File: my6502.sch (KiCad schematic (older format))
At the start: 4 parts

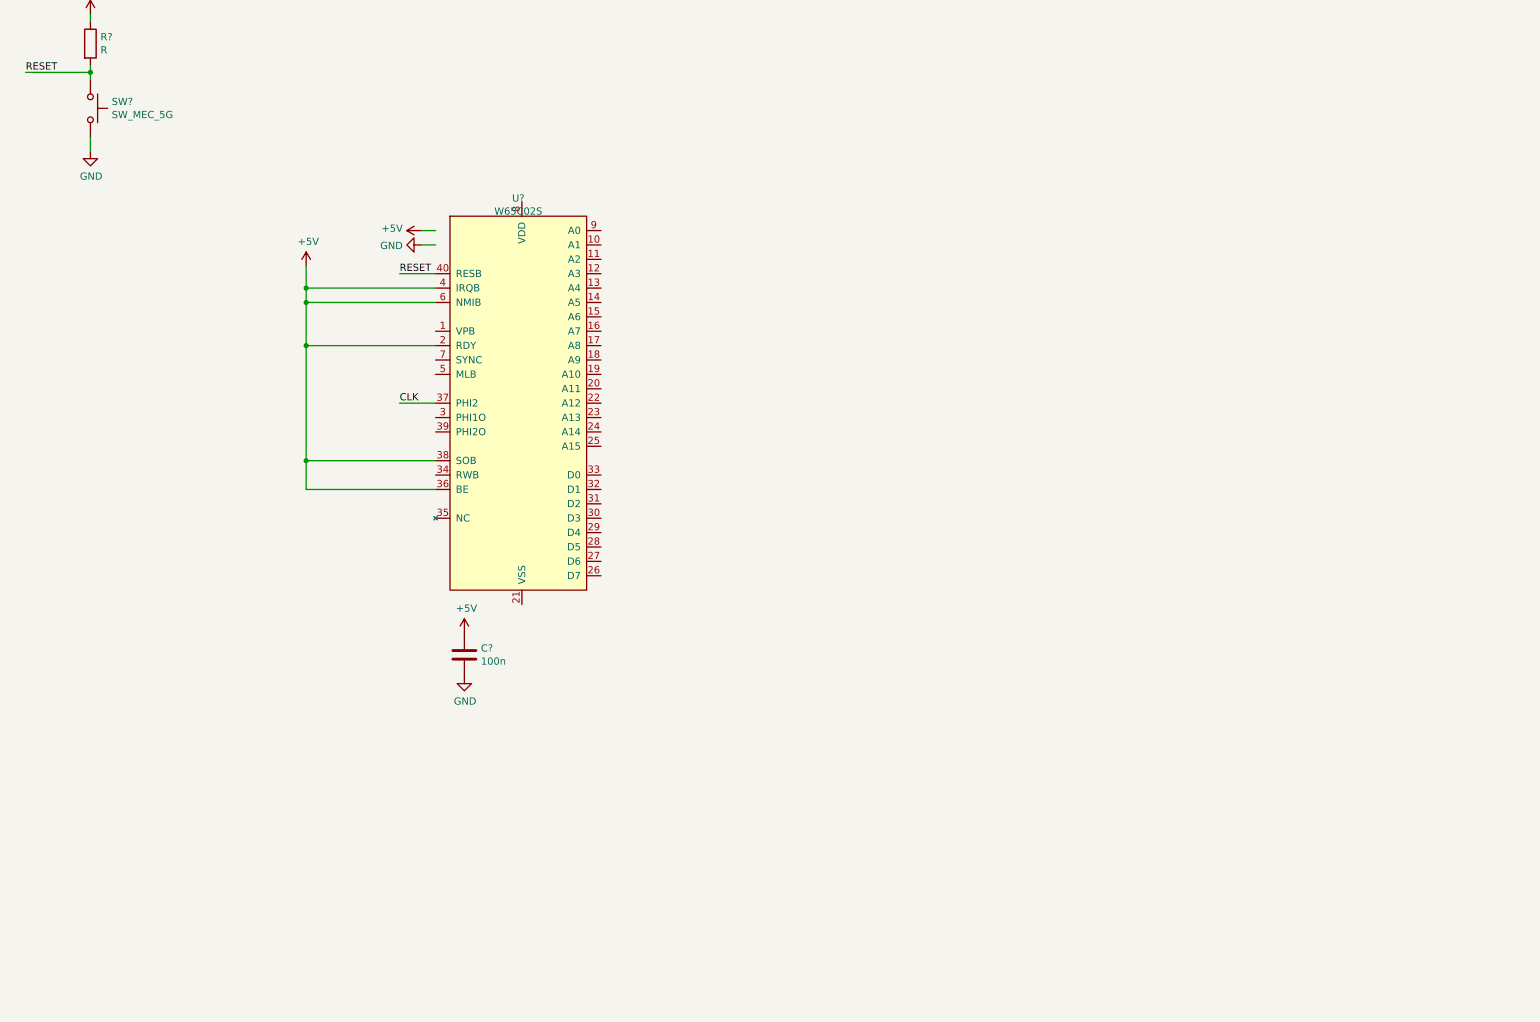
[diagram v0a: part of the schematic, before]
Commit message: Added VIA 65C22
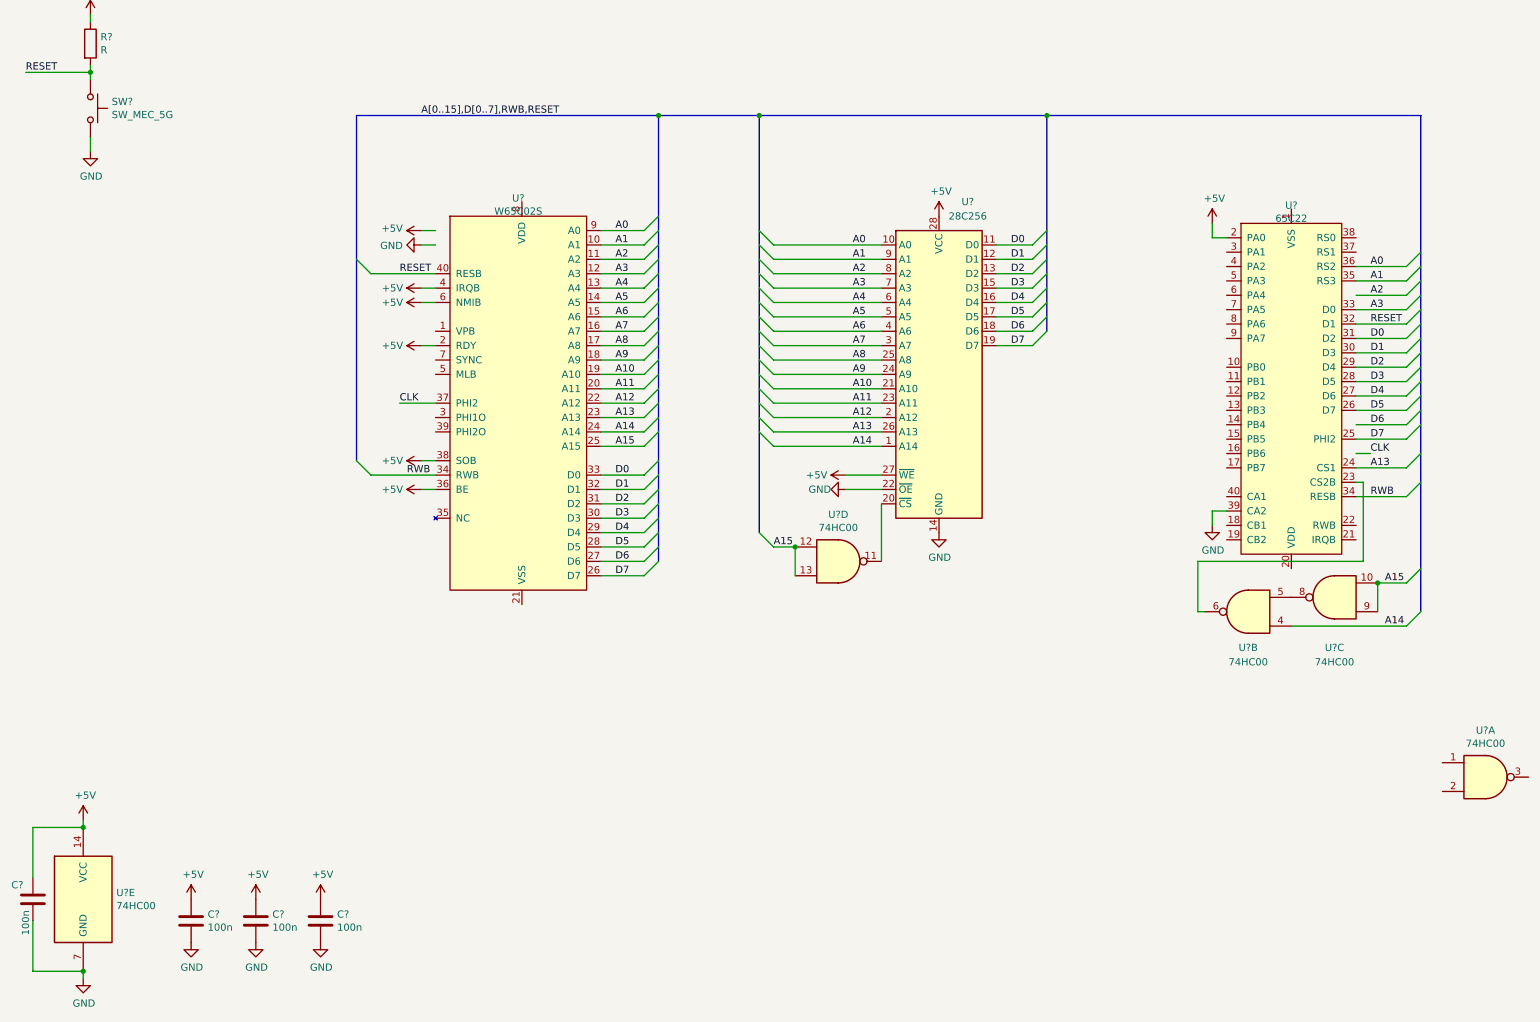
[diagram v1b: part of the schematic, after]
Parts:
- added C? (x3): 100n, symbol Device:C
- added U?: 28C256, symbol Memory_EEPROM:28C256
- added U? (x5): 74HC00, symbol 74xx:74HC00
- added U?: 65C22, symbol 6502:65C22
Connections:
- net labels added: A0, A1, A10, A11, A12, A13, A14, A15, A2, A3, A4, A5, A6, A7, A8, A9, A[0..15],D[0..7],RWB,RESET, D0, D1, D2, D3, D4, D5, D6, D7, RWB
- wire segments 19 -> 101
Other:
- moved on the sheet: C?

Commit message: Add RAM
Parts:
- removed U?: 74HC00, symbol 74xx:74HC00
- added C?: 100n, symbol Device:C
- added U?: CY62256-70PC, Package_DIP:DIP-28_W15.24mm, symbol Memory_RAM:CY62256-70PC
- added U?: 74HC00, symbol 74xx:74HC00
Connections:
- net labels added: ~A15
- wire segments 101 -> 141
- no-connect marks 0 -> 1
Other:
- moved on the sheet: R?, SW?, U?, U?A, U?B, U?D

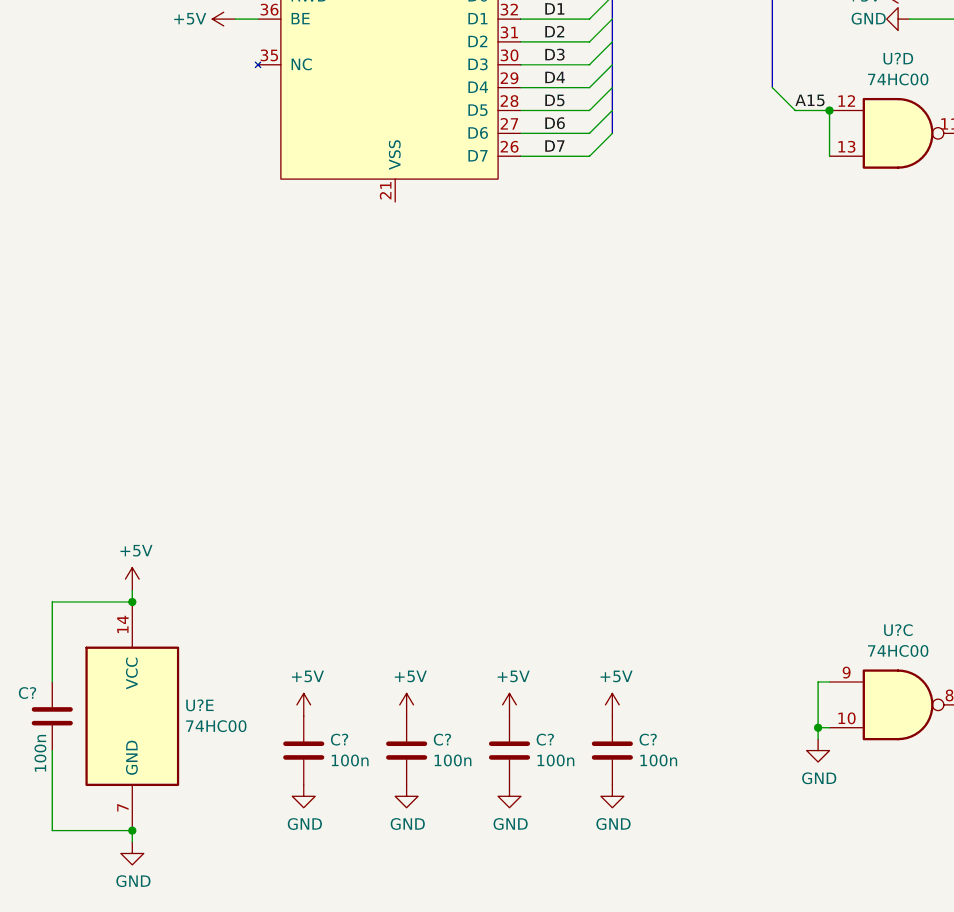
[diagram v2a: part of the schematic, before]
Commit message: Add minimal 555-based clock module
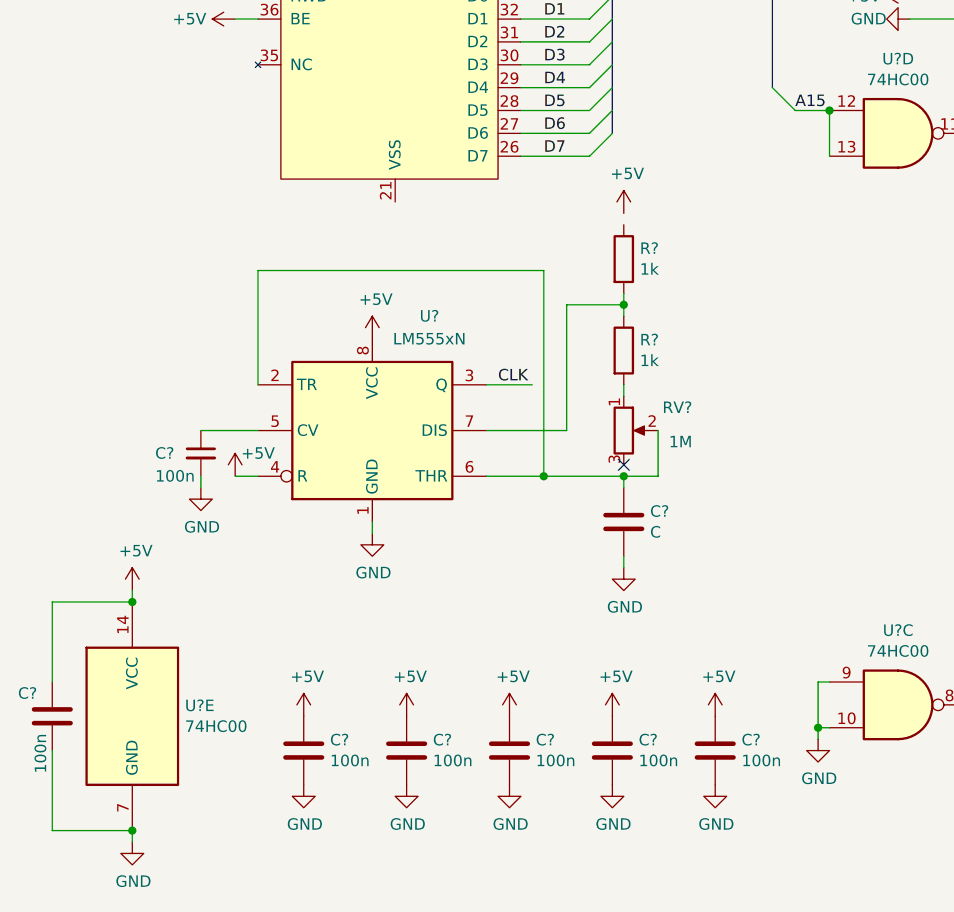
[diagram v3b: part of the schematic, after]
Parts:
- added C?: 100n, symbol Device:C
- added C?: 100n, symbol Device:C_Small
- added C?: C, symbol Device:C
- added R? (x2): 1k, symbol Device:R
- added RV?: 1M, symbol Device:R_POT
- added U?: LM555xN, Package_DIP:DIP-8_W7.62mm, symbol Timer:LM555xN
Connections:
- wire segments 141 -> 161
- no-connect marks 1 -> 2
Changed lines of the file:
@@
 Connection ~ 4050 7000
 NoConn ~ 4700 6900
+$Comp
+L Timer:LM555xN U?
+U 1 1 600B01EE
+P 2100 5700
+F 0 "U?" H 2350 6200 50  0000 C CNN
+F 1 "LM555xN" H 2350 6100 50  0000 C CNN
+F 2 "Package_DIP:DIP-8_W7.62mm" H 2750 5300 50  0001 C CNN
+F 3 "http://www.ti.com/lit/ds/symlink/lm555.pdf" H 2950 5300 50  0001 C CNN
+	1    2100 5700
+	1    0    0    -1
+$EndComp
+$Comp
+L power:+5V #PWR?
+U 1 1 600BEA22
+P 3200 4750
+F 0 "#PWR?" H 3200 4600 50  0001 C CNN
+F 1 "+5V" H 3215 4923 50  0000 C CNN
+F 2 "" H 3200 4750 50  0001 C CNN
+F 3 "" H 3200 4750 50  0001 C CNN
+	1    3200 4750
+	1    0    0    -1
+$EndComp
+Wire Wire Line
+	1600 5500 1600 5000
+Wire Wire Line
+	1600 5000 2850 5000
+Wire Wire Line
+	2850 5000 2850 5900
+$Comp
+L power:GND #PWR?
+U 1 1 601152B0
+P 3200 6300
+F 0 "#PWR?" H 3200 6050 50  0001 C CNN
+F 1 "GND" H 3205 6127 50  0000 C CNN
+F 2 "" H 3200 6300 50  0001 C CNN
+F 3 "" H 3200 6300 50  0001 C CNN
+	1    3200 6300
+	1    0    0    -1
+$EndComp
+$Comp
+L power:+5V #PWR?
+U 1 1 601169B4
+P 2100 5300
+F 0 "#PWR?" H 2100 5150 50  0001 C CNN
+F 1 "+5V" H 2115 5473 50  0000 C CNN
+F 2 "" H 2100 5300 50  0001 C CNN
+F 3 "" H 2100 5300 50  0001 C CNN
+	1    2100 5300
+	1    0    0    -1
+$EndComp
+$Comp
+L power:GND #PWR?
+U 1 1 6011DD9C
+P 2100 6150
+F 0 "#PWR?" H 2100 5900 50  0001 C CNN
+F 1 "GND" H 2105 5977 50  0000 C CNN
+F 2 "" H 2100 6150 50  0001 C CNN
+F 3 "" H 2100 6150 50  0001 C CNN
+	1    2100 6150
+	1    0    0    -1
+$EndComp
+$Comp
+L power:+5V #PWR?
+U 1 1 6012E6E9
+P 3600 6950
+F 0 "#PWR?" H 3600 6800 50  0001 C CNN
+F 1 "+5V" H 3615 7123 50  0000 C CNN
+F 2 "" H 3600 6950 50  0001 C CNN
+F 3 "" H 3600 6950 50  0001 C CNN
+	1    3600 6950
+	1    0    0    -1
+$EndComp
+$Comp
+L power:GND #PWR?
+U 1 1 6012EA99
+P 3600 7250
+F 0 "#PWR?" H 3600 7000 50  0001 C CNN
+F 1 "GND" H 3605 7077 50  0000 C CNN
+F 2 "" H 3600 7250 50  0001 C CNN
+F 3 "" H 3600 7250 50  0001 C CNN
+	1    3600 7250
+	1    0    0    -1
+$EndComp
+$Comp
+L Device:C C?
+U 1 1 6012EAA3
+P 3600 7100
+F 0 "C?" H 3715 7146 50  0000 L CNN
+F 1 "100n" H 3715 7055 50  0000 L CNN
+F 2 "" H 3638 6950 50  0001 C CNN
+F 3 "~" H 3600 7100 50  0001 C CNN
+	1    3600 7100
+	1    0    0    -1
+$EndComp
+$Comp
+L Device:C_Small C?
+U 1 1 6018E46C
+P 1350 5800
+F 0 "C?" H 1150 5800 50  0000 L CNN
+F 1 "100n" H 1150 5700 50  0000 L CNN
+F 2 "" H 1350 5800 50  0001 C CNN
+F 3 "~" H 1350 5800 50  0001 C CNN
+	1    1350 5800
+	1    0    0    -1
+$EndComp
+$Comp
+L power:GND #PWR?
+U 1 1 6018F461
+P 1350 5950
+F 0 "#PWR?" H 1350 5700 50  0001 C CNN
+F 1 "GND" H 1355 5777 50  0000 C CNN
+F 2 "" H 1350 5950 50  0001 C CNN
+F 3 "" H 1350 5950 50  0001 C CNN
+	1    1350 5950
+	1    0    0    -1
+$EndComp
+Wire Wire Line
+	1350 5700 1600 5700
+Wire Wire Line
+	1350 5900 1350 5950
+$Comp
+L power:+5V #PWR?
+U 1 1 601B5080
+P 1500 5900
+F 0 "#PWR?" H 1500 5750 50  0001 C CNN
+F 1 "+5V" H 1600 6000 50  0000 C CNN
+F 2 "" H 1500 5900 50  0001 C CNN
+F 3 "" H 1500 5900 50  0001 C CNN
+	1    1500 5900
+	1    0    0    -1
+$EndComp
+Wire Wire Line
+	1500 5900 1600 5900
+Wire Wire Line
+	2100 6100 2100 6150
+$Comp
+L Device:R_POT RV?
+U 1 1 601E869A
+P 3200 5700
+F 0 "RV?" H 3500 5800 50  0000 R CNN
+F 1 "1M" H 3500 5650 50  0000 R CNN
+F 2 "" H 3200 5700 50  0001 C CNN
+F 3 "~" H 3200 5700 50  0001 C CNN
+	1    3200 5700
+	1    0    0    -1
+$EndComp
+$Comp
+L Device:R R?
+U 1 1 601F2A63
+P 3200 5350
+F 0 "R?" H 3270 5396 50  0000 L CNN
+F 1 "1k" H 3270 5305 50  0000 L CNN
+F 2 "" V 3130 5350 50  0001 C CNN
+F 3 "~" H 3200 5350 50  0001 C CNN
+	1    3200 5350
+	1    0    0    -1
+$EndComp
+$Comp
+L Device:R R?
+U 1 1 601F2D27
+P 3200 4950
+F 0 "R?" H 3270 4996 50  0000 L CNN
+F 1 "1k" H 3270 4905 50  0000 L CNN
+F 2 "" V 3130 4950 50  0001 C CNN
+F 3 "~" H 3200 4950 50  0001 C CNN
+	1    3200 4950
+	1    0    0    -1
+$EndComp
+Wire Wire Line
+	2600 5900 2850 5900
+$Comp
+L Device:C C?
+U 1 1 601F897F
+P 3200 6100
+F 0 "C?" H 3315 6146 50  0000 L CNN
+F 1 "C" H 3315 6055 50  0000 L CNN
+F 2 "" H 3238 5950 50  0001 C CNN
+F 3 "~" H 3200 6100 50  0001 C CNN
+	1    3200 6100
+	1    0    0    -1
+$EndComp
+Wire Wire Line
+	3200 6250 3200 6300
+Wire Wire Line
+	3200 5500 3200 5550
+Wire Wire Line
+	3200 5100 3200 5150
+Wire Wire Line
+	3350 5700 3350 5900
+Wire Wire Line
+	3350 5900 3200 5900
+Wire Wire Line
+	3200 5900 3200 5950
+NoConn ~ 3200 5850
+Wire Wire Line
+	2600 5700 2950 5700
+Wire Wire Line
+	2950 5150 3200 5150
+Connection ~ 3200 5150
+Wire Wire Line
+	3200 5150 3200 5200
+Wire Wire Line
+	2950 5150 2950 5700
+Wire Wire Line
+	2850 5900 3200 5900
+Connection ~ 2850 5900
+Connection ~ 3200 5900
+Wire Wire Line
+	2600 5500 2800 5500
 Wire Bus Line
 	1050 1300 1050 3700
@@
 Wire Bus Line
 	3150 1300 3150 4400
+Text Label 2650 5500 0    50   ~ 0
+CLK
 $EndSCHEMATC
